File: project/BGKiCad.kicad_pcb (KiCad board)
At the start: 2 copper layers, 114.3 x 50.8 mm, 10 parts, among them J1 Alt. Power, J2 SWD, SW1 SW_Choc_v1_HS_CPG135001S30_1u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, SW2 SW_Choc_v1_HS_CPG135001S30_1.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, SW3 SW_Choc_v1_HS_CPG135001S30_1.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

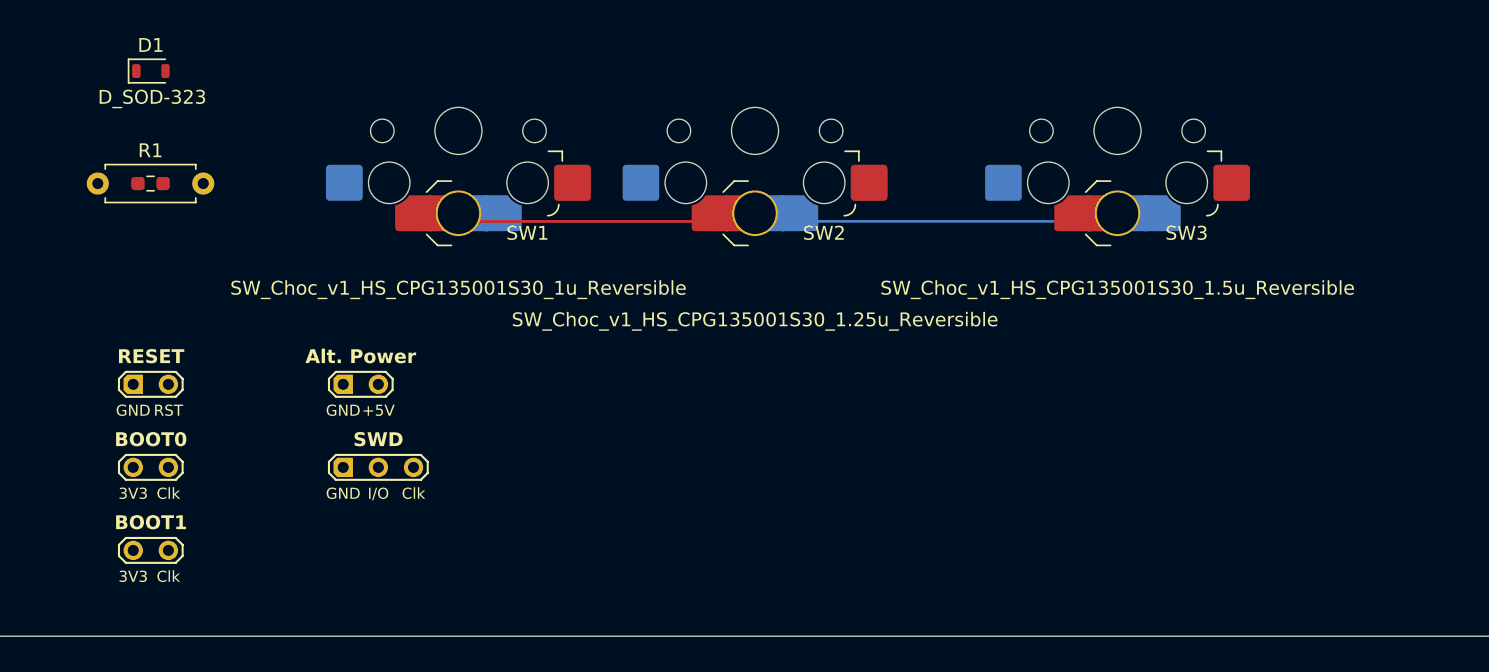
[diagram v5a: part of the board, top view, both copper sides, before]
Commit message: Remove unmasking of plated hole ring
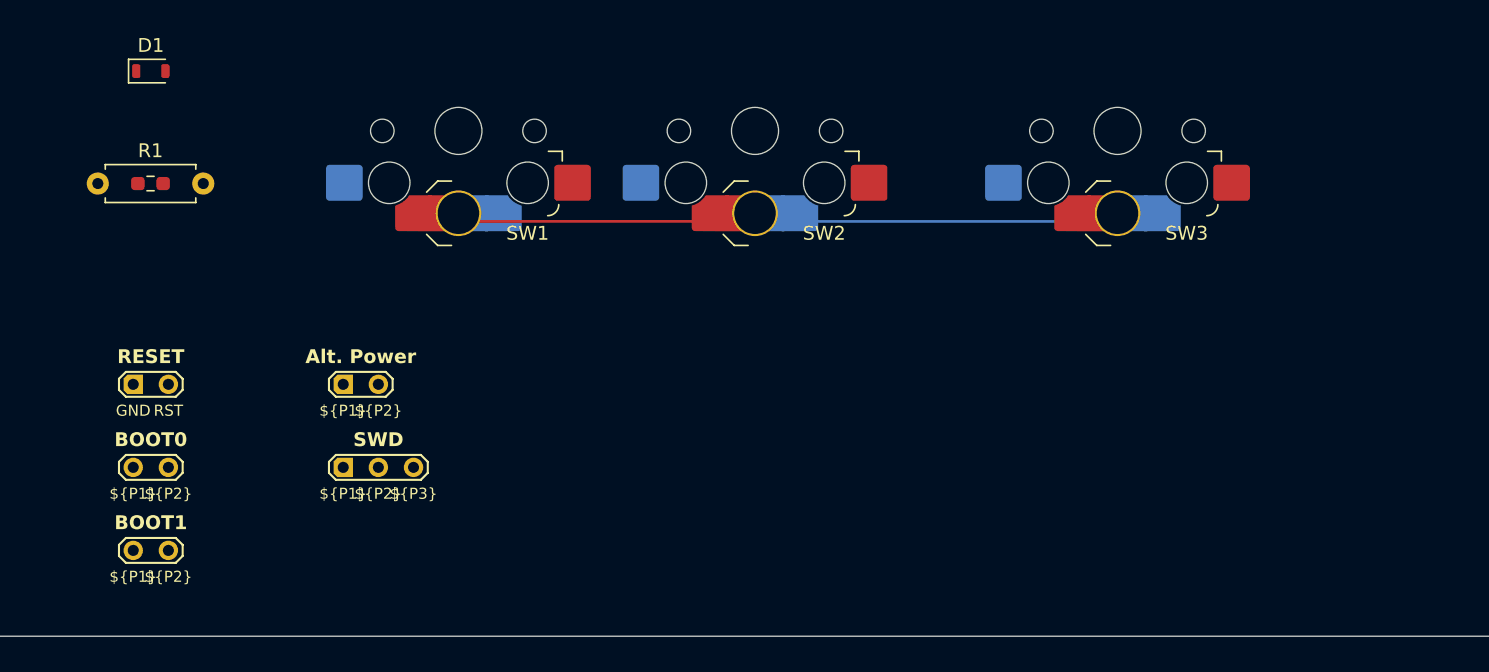
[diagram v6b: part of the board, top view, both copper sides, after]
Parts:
- SW1: value SW_Choc_v1_HS_CPG135001S30_1u_Reversible -> CPG135001S30
- SW2: value SW_Choc_v1_HS_CPG135001S30_1.25u_Reversible -> CPG135001S30
- SW3: value SW_Choc_v1_HS_CPG135001S30_1.5u_Reversible -> CPG135001S30

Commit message: Rename reversible Choc footprints
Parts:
- SW1: value CPG135001S30 -> SW_Choc_v1_HS_CPG135001S30_1u_Reversible; footprint BGKiCad:SW_Choc_v1_HS_CPG135001S30_1u_Reversible -> BGK_Kicad:SW_Choc_v1_HS_CPG135001S30_1u_Reversible_CtrPlt
- SW2: value CPG135001S30 -> SW_Choc_v1_HS_CPG135001S30_1.25u_Reversible; footprint BGKiCad:SW_Choc_v1_HS_CPG135001S30_1.25u_Reversible -> BGK_Kicad:SW_Choc_v1_HS_CPG135001S30_1.25u_Reversible_CtrPlt
- SW3: value CPG135001S30 -> SW_Choc_v1_HS_CPG135001S30_1.5u_Reversible; footprint BGKiCad:SW_Choc_v1_HS_CPG135001S30_1.5u_Reversible -> BGK_Kicad:SW_Choc_v1_HS_CPG135001S30_1.5u_Reversible_CtrPlt

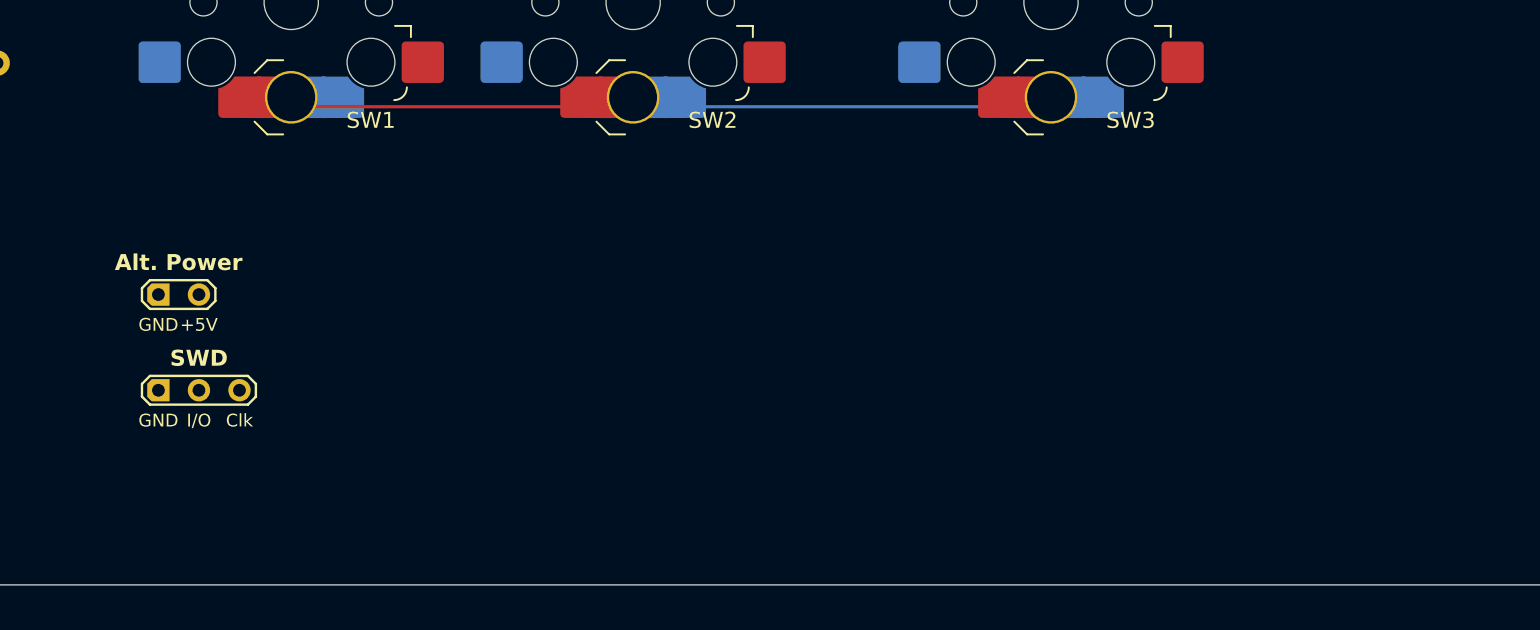
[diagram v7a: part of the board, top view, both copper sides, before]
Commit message: Update schematic and PCB with new footprints
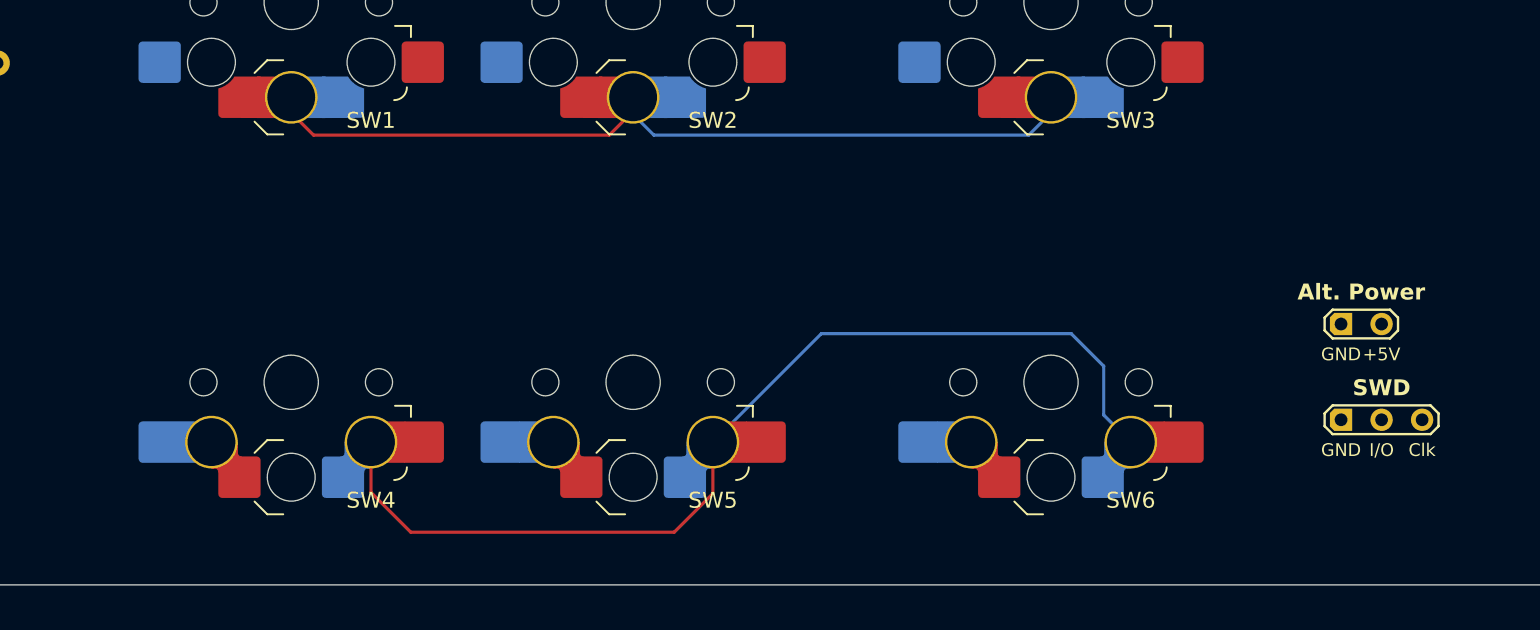
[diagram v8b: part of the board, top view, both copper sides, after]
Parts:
- added SW4: SW_Choc_v1_HS_CPG135001S30_Reversible_OutPlt_1u, BGKiCadDemo:SW_Choc_v1_HS_CPG135001S30_Reversible_OutPlt_1u, F.Cu at (60.3, 63.5)
- added SW5: SW_Choc_v1_HS_CPG135001S30_Reversible_OutPlt_1.25u, BGKiCadDemo:SW_Choc_v1_HS_CPG135001S30_Reversible_OutPlt_1.25u, F.Cu at (81.8, 63.5)
- added SW6: SW_Choc_v1_HS_CPG135001S30_Reversible_OutPlt_1.5u, BGKiCadDemo:SW_Choc_v1_HS_CPG135001S30_Reversible_OutPlt_1.5u, F.Cu at (108.0, 63.5)
- D1: footprint BGKiCad:D_SOD-323 -> BGKiCadDemo:D_SOD-323
- J1: footprint BGK_Kicad:TestPoint_2LabelledPads_Pitch2.54mm_Drill0.8mm -> BGKiCadDemo:TestPoint_2LabelledPads_Pitch2.54mm_Drill0.8mm
- J2: footprint BGK_Kicad:TestPoint_3LabelledPads_Pitch2.54mm_Drill0.8mm -> BGKiCadDemo:TestPoint_3LabelledPads_Pitch2.54mm_Drill0.8mm
- R1: footprint BGK_Kicad:R_Combined_Axial_DIN0207_0603_1608Metric -> BGKiCadDemo:R_Combined_Axial_DIN0207_0603_1608Metric
- SW1: value SW_Choc_v1_HS_CPG135001S30_1u_Reversible -> SW_Choc_v1_HS_CPG135001S30_Reversible_CtrPlt_1u; footprint BGK_Kicad:SW_Choc_v1_HS_CPG135001S30_1u_Reversible_CtrPlt -> BGKiCadDemo:SW_Choc_v1_HS_CPG135001S30_Reversible_CtrPlt_1u
- SW2: value SW_Choc_v1_HS_CPG135001S30_1.25u_Reversible -> SW_Choc_v1_HS_CPG135001S30_Reversible_CtrPlt_1.25u; footprint BGK_Kicad:SW_Choc_v1_HS_CPG135001S30_1.25u_Reversible_CtrPlt -> BGKiCadDemo:SW_Choc_v1_HS_CPG135001S30_Reversible_CtrPlt_1.25u
- SW3: value SW_Choc_v1_HS_CPG135001S30_1.5u_Reversible -> SW_Choc_v1_HS_CPG135001S30_Reversible_CtrPlt_1.5u; footprint BGK_Kicad:SW_Choc_v1_HS_CPG135001S30_1.5u_Reversible_CtrPlt -> BGKiCadDemo:SW_Choc_v1_HS_CPG135001S30_Reversible_CtrPlt_1.5u
- TP1: footprint BGK_Kicad:ResetJumper_Pitch2.54mm_Drill0.8mm -> BGKiCadDemo:ResetJumper_Pitch2.54mm_Drill0.8mm
- TP2: footprint BGKiCad:BootJumper_Pitch2.54mm_Drill0.8mm -> BGKiCadDemo:BootJumper_Pitch2.54mm_Drill0.8mm
- TP3: footprint BGKiCad:BootJumper_Alt_Pitch2.54mm_Drill0.8mm -> BGKiCadDemo:BootJumper_Alt_Pitch2.54mm_Drill0.8mm
- moved J1 74.2 mm to (126.1, 59.8)
- moved J2 74.2 mm to (126.1, 65.8)
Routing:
- net Net-(SW4-Pad2): track 0.00 -> 63.5 mm
- net Net-(SW1-Pad2): track 48.6 -> 53.8 mm
